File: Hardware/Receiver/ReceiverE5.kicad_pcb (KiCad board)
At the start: 4 copper layers, 50 x 30 mm, 42 parts, among them J1 KBUS, J2 AVR-PDI-6A, J3 CONN_01X08, J4 CONN_01X06, J5 CONN_01X06, J6 CONN_01X04, J7 CONN_01X04, U1 ATXMEGA32E5-A, U2 LM2731, U3 SN74LV07A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

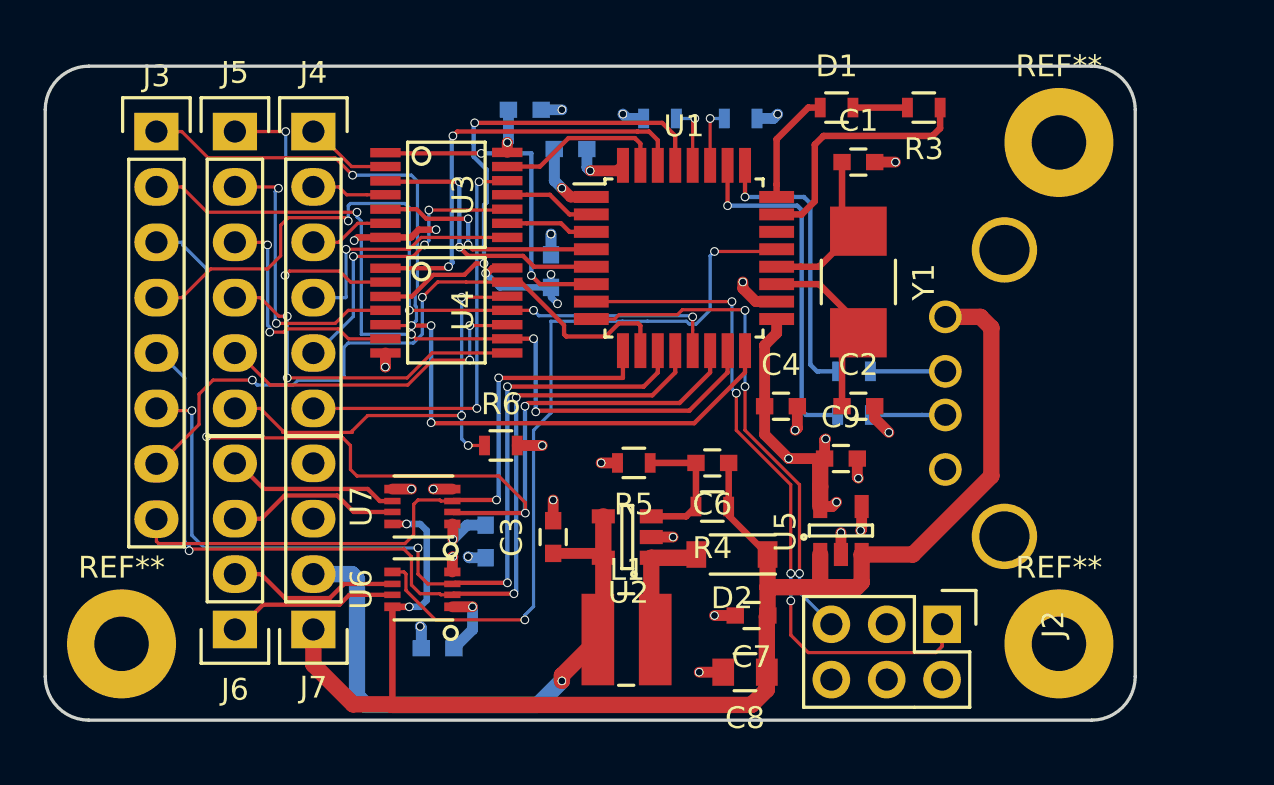
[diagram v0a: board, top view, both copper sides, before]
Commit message: Passed DRC again
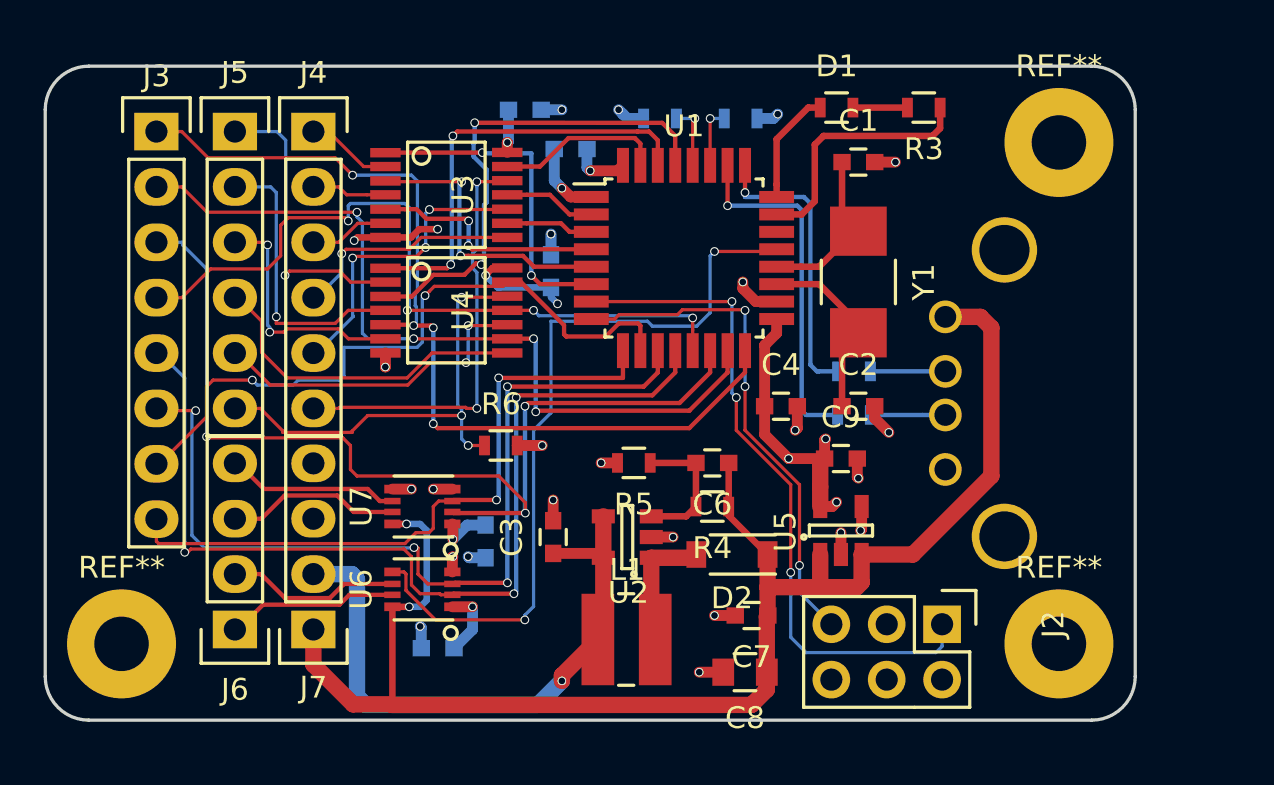
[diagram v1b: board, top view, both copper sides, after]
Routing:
- net Net-(J2-Pad1): track 32.5 -> 31.4 mm, vias 4 -> 3
- net Net-(J5-Pad4): track 16.1 -> 15.3 mm, vias 2 -> 0
- net Net-(J4-Pad4): track 11.3 -> 10.6 mm
- net +3V3: track 30.1 -> 29.5 mm, vias 11 -> 10
- net Net-(J5-Pad2): track 13.6 -> 13.3 mm, vias 2 -> 1
- net Net-(J5-Pad1): track 13.8 -> 13.6 mm, vias 2 -> 1

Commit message: USB connector was on wrong side of the board
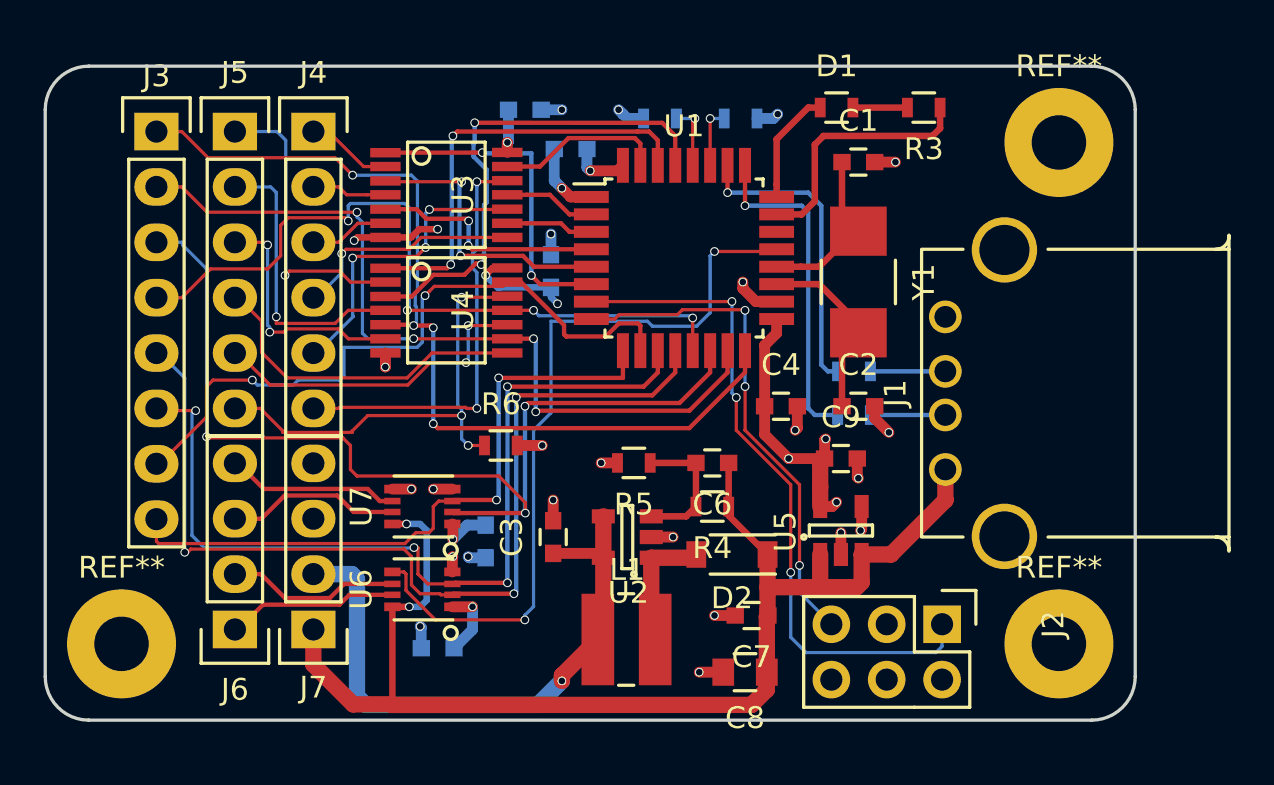
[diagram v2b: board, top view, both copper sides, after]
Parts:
- J1: moved to F.Cu
- moved R7 2.00 mm to (104.1, 79.0)
- moved R8 2.00 mm to (104.1, 77.0)
- turned J1 to 90 degrees
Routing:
- net +5V: track 69.5 -> 59.3 mm
- net /KBUS_RX: track 16.3 -> 14.0 mm
- net /KBUS_TX: track 13.3 -> 15.3 mm

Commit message: Silk + mounting holes changed to M2.5
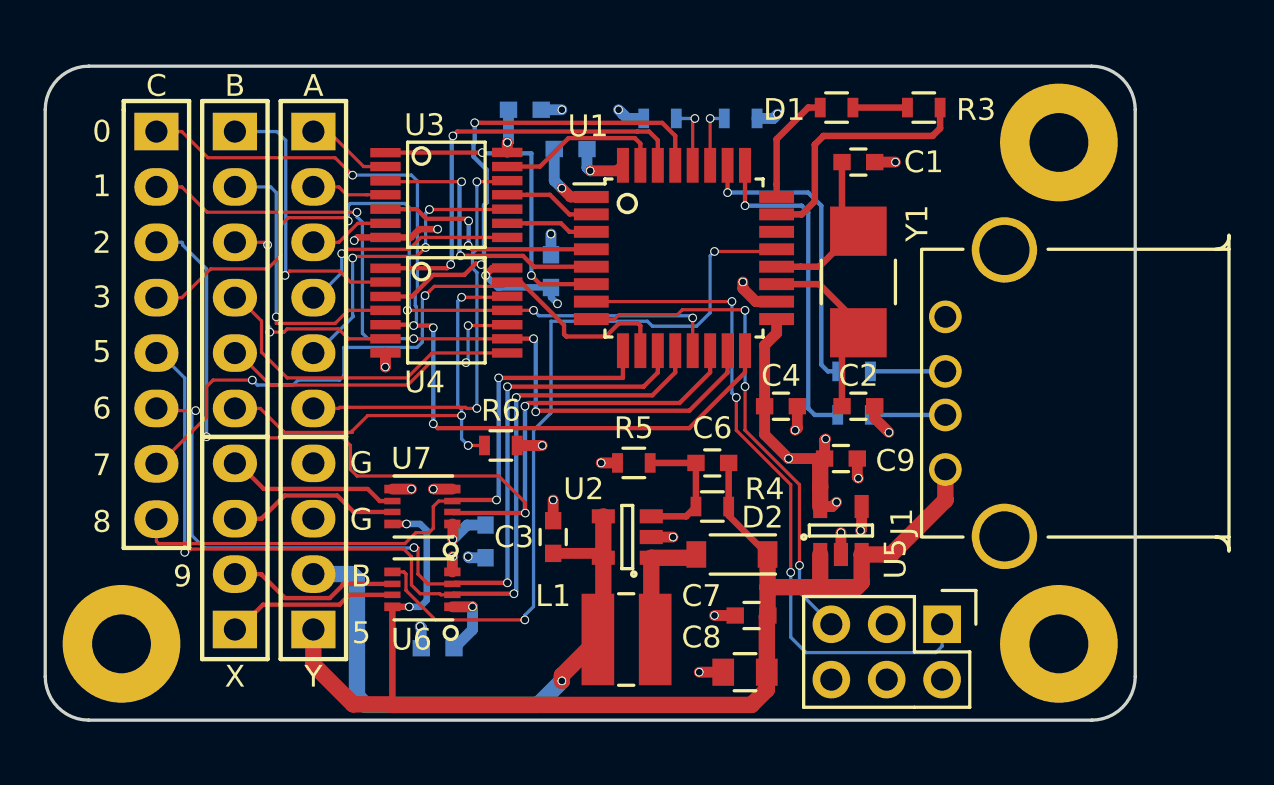
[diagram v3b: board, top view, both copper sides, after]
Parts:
- REF** (x3): footprint Mounting_Holes:MountingHole_2.5mm_Pad -> Mounting_Holes:MountingHole_2.7mm_M2.5_Pad
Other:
- board text added: "0"
- board text added: "1"
- board text added: "2"
- board text added: "3"
- board text added: "5"
- board text added: "6"
- board text added: "7"
- board text added: "8"
- board text added: "9"
- board text added: "A"
- board text added: "B"
- board text added: "C"
- board text added: "G"
- board text added: "X"
- board text added: "Y"
